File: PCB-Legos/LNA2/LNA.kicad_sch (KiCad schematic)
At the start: 35 parts, among them J1 Conn_Coaxial, J2 Conn_Coaxial, J3 Conn_Coaxial, U1 LP2985XX-N, U2 LNA-TP3M9037, U3 QPQ1907, U4 LP2985XX-N, U5 LNA-TP3M9037, U6 QPQ1907

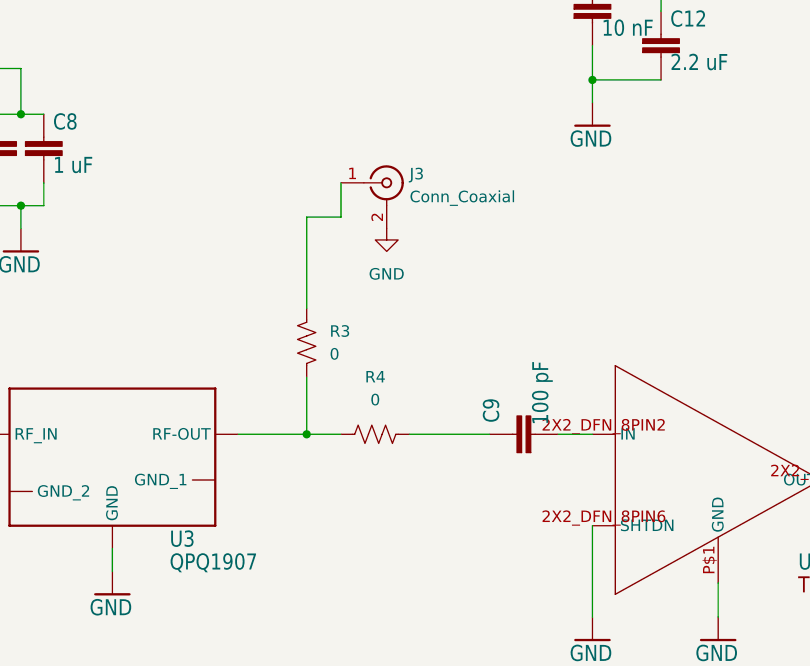
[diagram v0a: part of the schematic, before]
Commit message: LNA
Fixed minor issues in RF path.
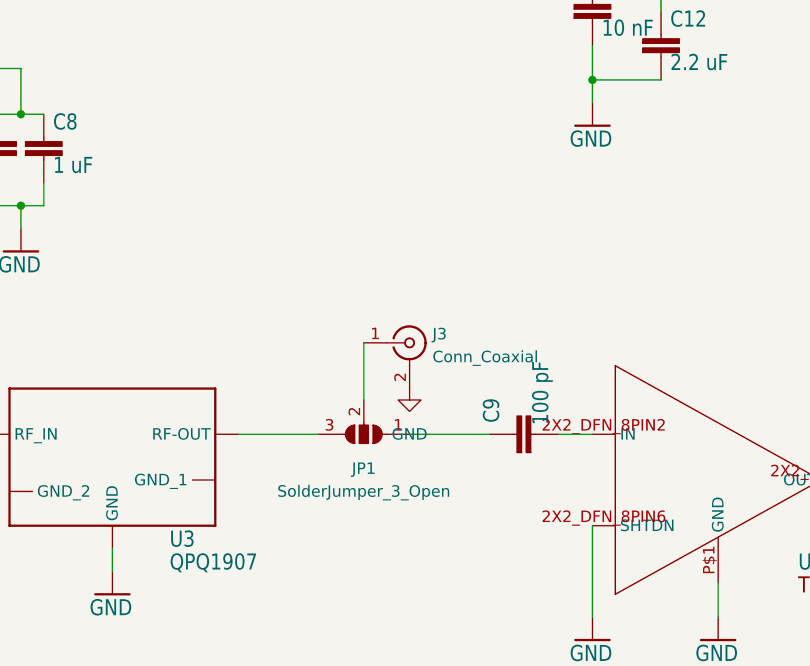
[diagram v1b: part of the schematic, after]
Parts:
- removed R3, R4: 0, HGS_Reflector:.0603-B-NOSILK, symbol Device:R_US
- added JP1: SolderJumper_3_Open, Jumper:SolderJumper-3_P1.3mm_Open_Pad1.0x1.5mm_NumberLabels, symbol Jumper:SolderJumper_3_Open
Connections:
- net at U3.OUTPUT (RF-OUT): now also JP1.3 (B)
- net at C9.1: now also JP1.1 (A)
- net at J3.1 (In): now also JP1.2 (C)
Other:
- moved on the sheet: J3
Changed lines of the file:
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@@
   (junction (at 160.02 54.61) (diameter 0) (color 0 0 0 0)
   )
-  (junction (at 135.89 127) (diameter 0) (color 0 0 0 0)
-  )
   (junction (at 212.09 91.44) (diameter 0) (color 0 0 0 0)
   )
@@
     (stroke (width 0) (type default) (color 0 0 0 0))
   )
-  (wire (pts (xy 128.27 127) (xy 135.89 127))
+  (wire (pts (xy 128.27 127) (xy 137.16 127))
     (stroke (width 0) (type default) (color 0 0 0 0))
   )
@@
     (stroke (width 0) (type default) (color 0 0 0 0))
   )
-  (wire (pts (xy 139.7 99.06) (xy 139.7 102.87))
-    (stroke (width 0) (type default) (color 0 0 0 0))
-  )
   (wire (pts (xy 224.79 144.78) (xy 224.79 147.32))
     (stroke (width 0) (type default) (color 0 0 0 0))
@@
     (stroke (width 0) (type default) (color 0 0 0 0))
   )
-  (wire (pts (xy 135.89 120.65) (xy 135.89 127))
-    (stroke (width 0) (type default) (color 0 0 0 0))
-  )
   (wire (pts (xy 59.69 90.17) (xy 59.69 87.63))
     (stroke (width 0) (type default) (color 0 0 0 0))
@@
     (stroke (width 0) (type default) (color 0 0 0 0))
   )
-  (wire (pts (xy 139.7 102.87) (xy 135.89 102.87))
-    (stroke (width 0) (type default) (color 0 0 0 0))
-  )
   (wire (pts (xy 147.32 127) (xy 156.21 127))
     (stroke (width 0) (type default) (color 0 0 0 0))
@@
     (stroke (width 0) (type default) (color 0 0 0 0))
   )
+  (wire (pts (xy 142.24 116.84) (xy 142.24 123.19))
+    (stroke (width 0) (type default) (color 0 0 0 0))
+  )
   (wire (pts (xy 167.64 44.45) (xy 167.64 40.64))
     (stroke (width 0) (type default) (color 0 0 0 0))
@@
   )
   (wire (pts (xy 88.9 86.36) (xy 95.25 86.36))
-    (stroke (width 0) (type default) (color 0 0 0 0))
-  )
-  (wire (pts (xy 135.89 102.87) (xy 135.89 113.03))
-    (stroke (width 0) (type default) (color 0 0 0 0))
-  )
-  (wire (pts (xy 135.89 127) (xy 139.7 127))
     (stroke (width 0) (type default) (color 0 0 0 0))
   )
@@
     (pin "OUTPUT")
   )
-  (symbol (lib_id "power:GND") (at 144.78 104.14 0) (unit 1)
+  (symbol (lib_id "power:GND") (at 147.32 121.92 0) (unit 1)
     (in_bom yes) (on_board yes) (fields_autoplaced)
-    (property "Reference" "#PWR0102" (id 0) (at 144.78 110.49 0)
-      (effects (font (size 1.27 1.27)) hide)
-    )
-    (property "Value" "GND" (id 1) (at 144.78 109.22 0))
-    (property "Footprint" "" (id 2) (at 144.78 104.14 0)
-      (effects (font (size 1.27 1.27)) hide)
-    )
-    (property "Datasheet" "" (id 3) (at 144.78 104.14 0)
+    (property "Reference" "#PWR0102" (id 0) (at 147.32 128.27 0)
+      (effects (font (size 1.27 1.27)) hide)
+    )
+    (property "Value" "GND" (id 1) (at 147.32 127 0))
+    (property "Footprint" "" (id 2) (at 147.32 121.92 0)
+      (effects (font (size 1.27 1.27)) hide)
+    )
+    (property "Datasheet" "" (id 3) (at 147.32 121.92 0)
       (effects (font (size 1.27 1.27)) hide)
     )
@@
     (pin "2")
   )
-  (symbol (lib_id "Device:R_US") (at 143.51 127 90) (unit 1)
-    (in_bom yes) (on_board yes) (fields_autoplaced)
-    (property "Reference" "R4" (id 0) (at 143.51 120.65 90))
-    (property "Value" "0" (id 1) (at 143.51 123.19 90))
-    (property "Footprint" "HGS_Reflector:.0603-B-NOSILK" (id 2) (at 143.764 125.984 90)
-      (effects (font (size 1.27 1.27)) hide)
-    )
-    (property "Datasheet" "~" (id 3) (at 143.51 127 0)
-      (effects (font (size 1.27 1.27)) hide)
-    )
-    (pin "1")
-    (pin "2")
-  )
   (symbol (lib_id "HGS_Reflector-eagle-import:GND") (at 224.79 149.86 0) (unit 1)
     (in_bom yes) (on_board yes)
@@
     (pin "2")
   )
-  (symbol (lib_id "Connector:Conn_Coaxial") (at 144.78 99.06 0) (unit 1)
+  (symbol (lib_id "Connector:Conn_Coaxial") (at 147.32 116.84 0) (unit 1)
     (in_bom yes) (on_board yes) (fields_autoplaced)
-    (property "Reference" "J3" (id 0) (at 147.32 98.0831 0)
+    (property "Reference" "J3" (id 0) (at 149.86 115.8631 0)
       (effects (font (size 1.27 1.27)) (justify left))
     )
-    (property "Value" "Conn_Coaxial" (id 1) (at 147.32 100.6231 0)
+    (property "Value" "Conn_Coaxial" (id 1) (at 149.86 118.4031 0)
       (effects (font (size 1.27 1.27)) (justify left))
     )
-    (property "Footprint" "Connector_Coaxial:SMA_Molex_73251-1153_EdgeMount_Horizontal" (id 2) (at 144.78 99.06 0)
-      (effects (font (size 1.27 1.27)) hide)
-    )
-    (property "Datasheet" " ~" (id 3) (at 144.78 99.06 0)
+    (property "Footprint" "Connector_Coaxial:SMA_Molex_73251-1153_EdgeMount_Horizontal" (id 2) (at 147.32 116.84 0)
+      (effects (font (size 1.27 1.27)) hide)
+    )
+    (property "Datasheet" " ~" (id 3) (at 147.32 116.84 0)
       (effects (font (size 1.27 1.27)) hide)
     )
@@
     )
     (pin "1")
+  )
+  (symbol (lib_id "Jumper:SolderJumper_3_Open") (at 142.24 127 180) (unit 1)
+    (in_bom yes) (on_board yes) (fields_autoplaced)
+    (property "Reference" "JP1" (id 0) (at 142.24 130.81 0))
+    (property "Value" "SolderJumper_3_Open" (id 1) (at 142.24 133.35 0))
+    (property "Footprint" "Jumper:SolderJumper-3_P1.3mm_Open_Pad1.0x1.5mm_NumberLabels" (id 2) (at 142.24 127 0)
+      (effects (font (size 1.27 1.27)) hide)
+    )
+    (property "Datasheet" "~" (id 3) (at 142.24 127 0)
+      (effects (font (size 1.27 1.27)) hide)
+    )
+    (pin "1")
+    (pin "2")
+    (pin "3")
   )
   (symbol (lib_id "HGS_Reflector-eagle-import:GND") (at 181.61 149.86 0) (unit 1)
@@
     )
     (pin "1")
-  )
-  (symbol (lib_id "Device:R_US") (at 135.89 116.84 0) (mirror y) (unit 1)
-    (in_bom yes) (on_board yes) (fields_autoplaced)
-    (property "Reference" "R3" (id 0) (at 138.43 115.5699 0)
-      (effects (font (size 1.27 1.27)) (justify right))
-    )
-    (property "Value" "0" (id 1) (at 138.43 118.1099 0)
-      (effects (font (size 1.27 1.27)) (justify right))
-    )
-    (property "Footprint" "HGS_Reflector:.0603-B-NOSILK" (id 2) (at 134.874 117.094 90)
-      (effects (font (size 1.27 1.27)) hide)
-    )
-    (property "Datasheet" "~" (id 3) (at 135.89 116.84 0)
-      (effects (font (size 1.27 1.27)) hide)
-    )
-    (pin "1")
-    (pin "2")
   )
   (symbol (lib_id "HGS_Reflector-eagle-import:C-EU0402-C-NOSILK") (at 201.93 132.08 90) (unit 1)
@@
       (reference "J3") (unit 1) (value "Conn_Coaxial") (footprint "Connector_Coaxial:SMA_Molex_73251-1153_EdgeMount_Horizontal")
     )
+    (path "/742f6656-c86d-41c0-937e-ef6ded3bd482"
+      (reference "JP1") (unit 1) (value "SolderJumper_3_Open") (footprint "Jumper:SolderJumper-3_P1.3mm_Open_Pad1.0x1.5mm_NumberLabels")
+    )
     (path "/29f4961c-cbd7-42a0-91e7-8ae77405e061"
       (reference "L1") (unit 1) (value "8n") (footprint "HGS_Reflector:L3216C")
@@
       (reference "R2") (unit 1) (value "0") (footprint "HGS_Reflector:.0603-B-NOSILK")
     )
-    (path "/ed452e4f-f8c6-4901-b871-cda6a9b3fcb3"
-      (reference "R3") (unit 1) (value "0") (footprint "HGS_Reflector:.0603-B-NOSILK")
-    )
-    (path "/226baf08-791d-4a76-8272-9455f91278e4"
-      (reference "R4") (unit 1) (value "0") (footprint "HGS_Reflector:.0603-B-NOSILK")
-    )
     (path "/a0af1aa5-82ff-4825-8836-86496e7db65f"
